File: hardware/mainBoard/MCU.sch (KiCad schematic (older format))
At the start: 7 parts

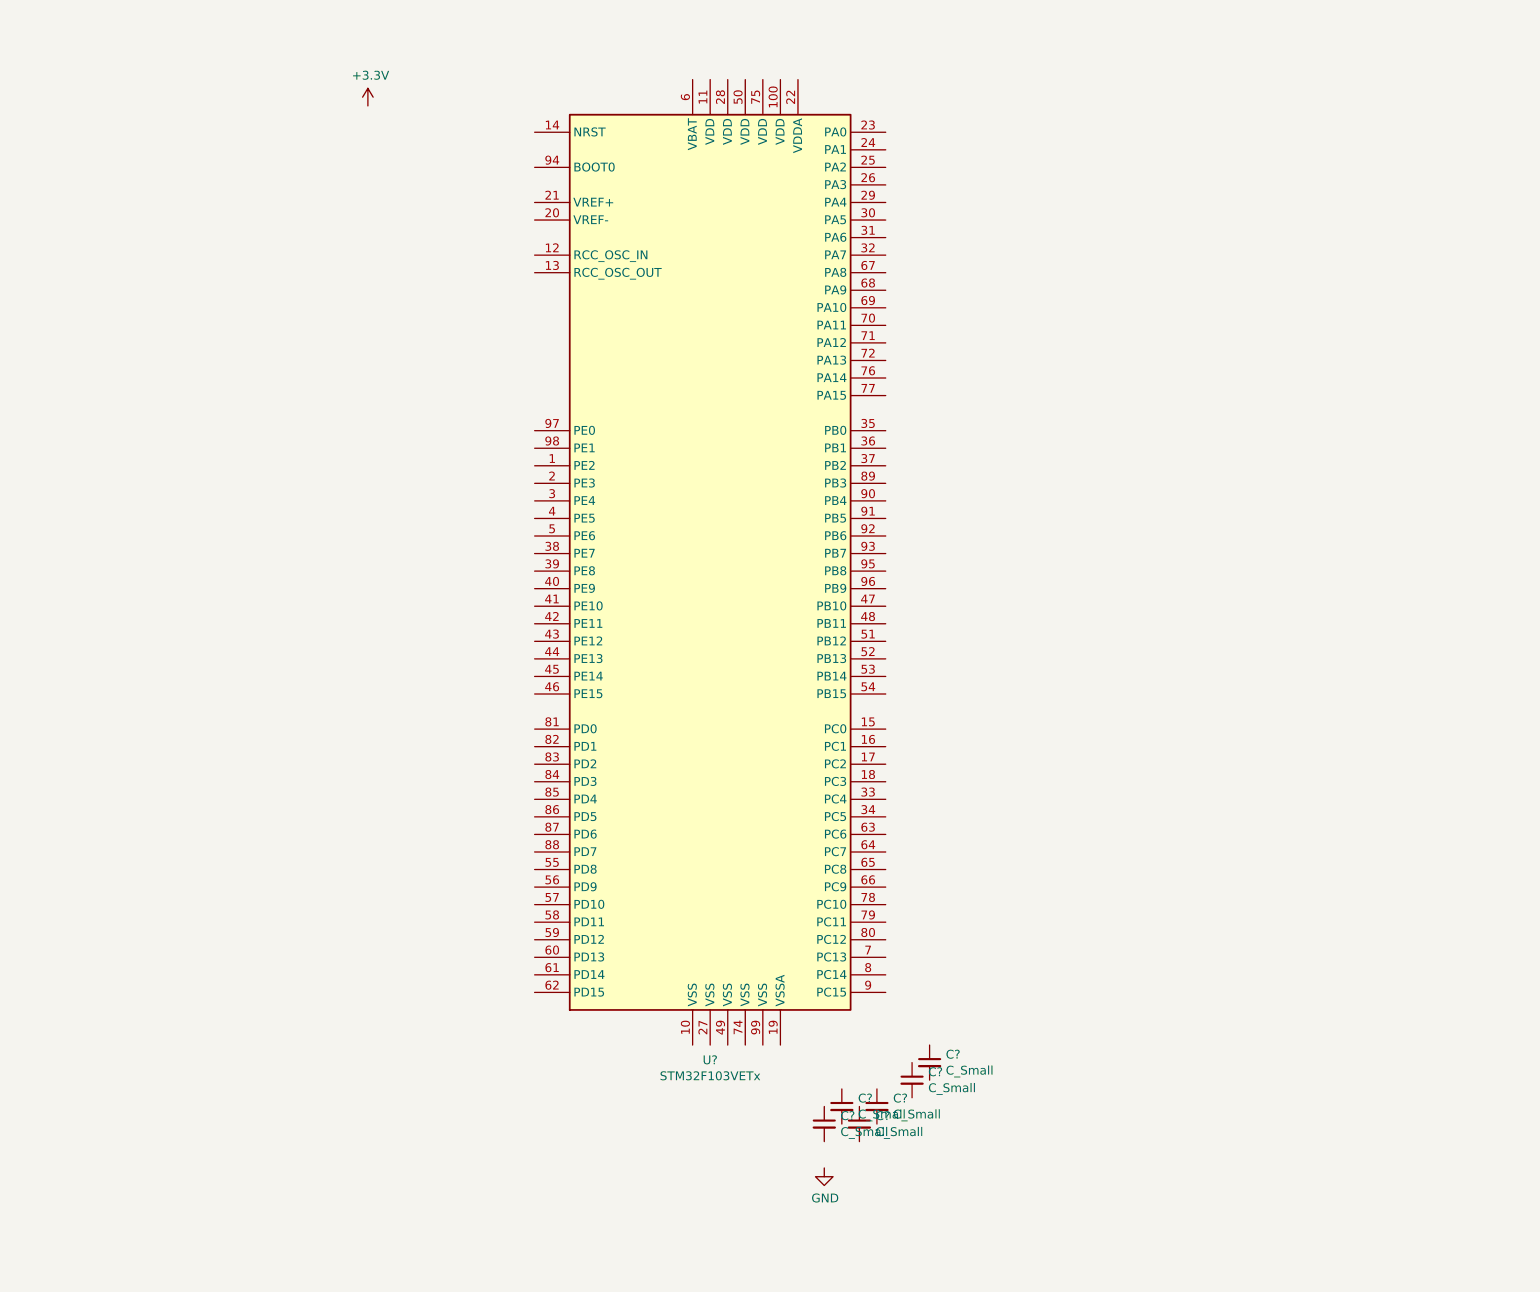
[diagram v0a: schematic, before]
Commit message: Added the power part of the schematic
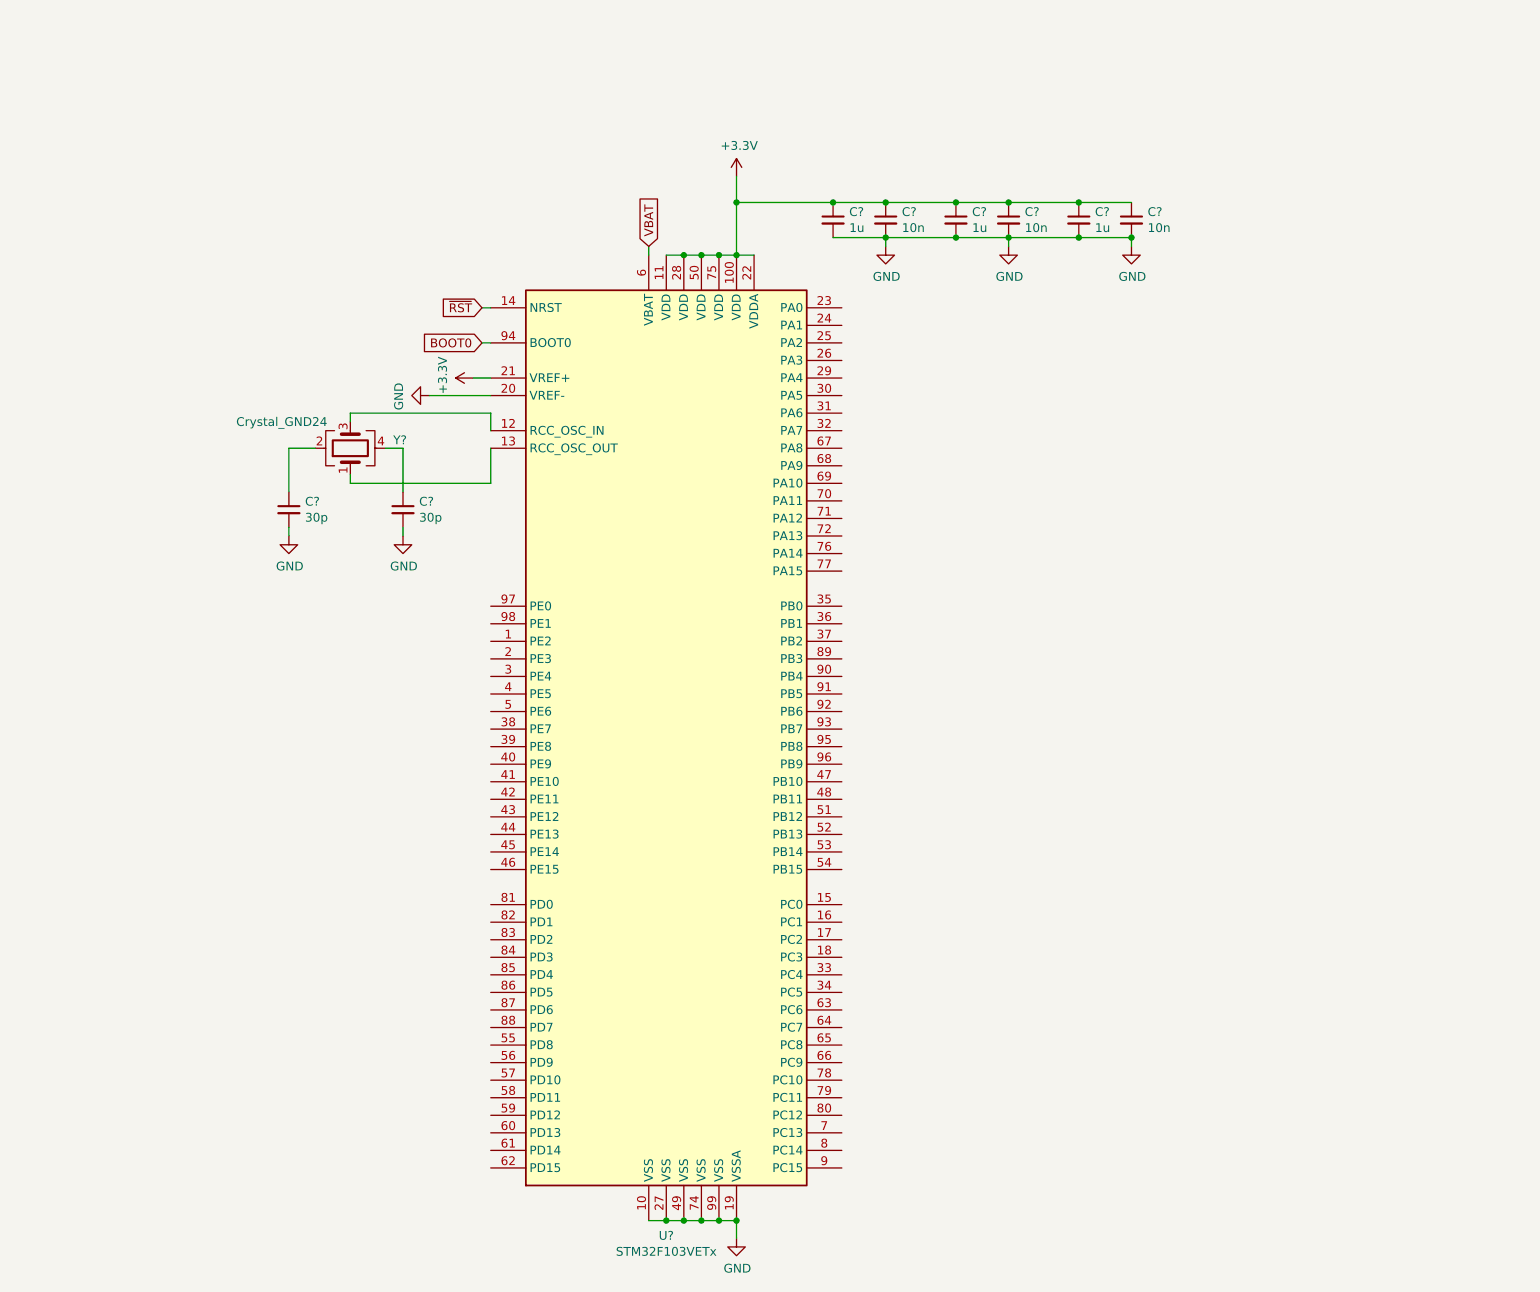
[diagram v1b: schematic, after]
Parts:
- removed C? (x5): C_Small, symbol Device:C_Small
- added C? (x3): 10n, symbol Device:C_Small
- added C? (x2): 1u, symbol Device:C_Small
- added C? (x2): 30p, symbol Device:C_Small
- added Y?: Crystal_GND24, symbol Device:Crystal_GND24
- C?: value C_Small -> 1u
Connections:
- net +3V3: now also C?.1, U?.100 (VDD), U?.11 (VDD), U?.21 (VREF+), U?.22 (VDDA), U?.28 (VDD), U?.50 (VDD), U?.75 (VDD), C?.1, C?.1, C?.1, C?.1, C?.1
- net GND: now also C?.2, U?.10 (VSS), U?.19 (VSSA), U?.20 (VREF-), U?.27 (VSS), U?.49 (VSS), U?.74 (VSS), U?.99 (VSS), C?.2, C?.2, C?.2, C?.2, C?.2, C?.2, C?.2
- net at U?.12 (RCC_OSC_IN): now also Y?.3
- net at U?.13 (RCC_OSC_OUT): now also Y?.1
- net ~RST: now reaches U?.14 (NRST)
- net VBAT: now reaches U?.6 (VBAT)
- net BOOT0: now reaches U?.94 (BOOT0)
- new net: C?.1, Y?.2
- new net: C?.1, Y?.4
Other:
- moved on the sheet: C?, U?

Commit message: Added external connections, analog conditioning and several items
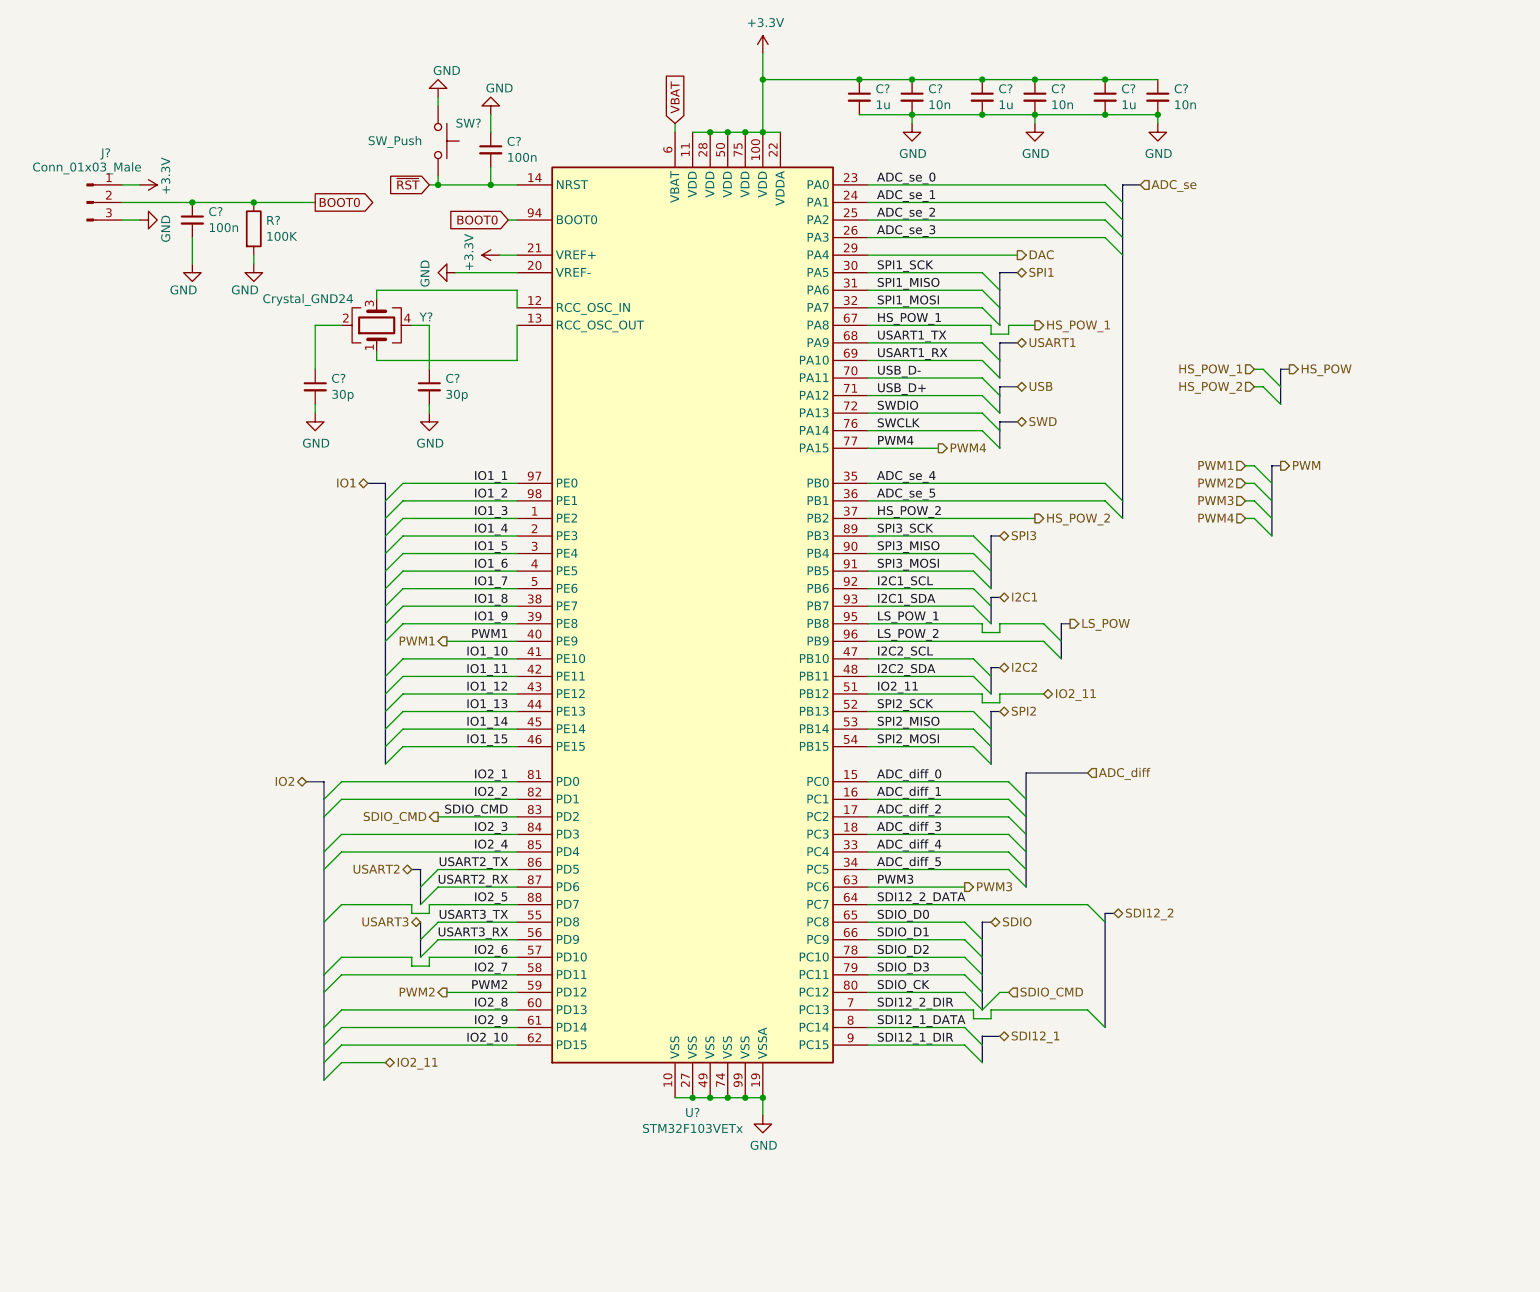
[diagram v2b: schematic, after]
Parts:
- added C? (x2): 100n, symbol Device:C_Small
- added J?: Conn_01x03_Male, symbol Connector:Conn_01x03_Male
- added R?: 100K, symbol Device:R
- added SW?: SW_Push, symbol Switch:SW_Push
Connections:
- net +3V3: now also J?.1 (Pin_1)
- net BOOT0: now also C?.1, J?.2 (Pin_2), R?.1
- net GND: now also C?.1, C?.2, J?.3 (Pin_3), R?.2, SW?.1
- net ~RST: now also C?.2, SW?.2
- net IO1_3: now reaches U?.1 (PE2)
- net ADC_diff_0: now reaches U?.15 (PC0)
- net ADC_diff_1: now reaches U?.16 (PC1)
- net ADC_diff_2: now reaches U?.17 (PC2)
- net ADC_diff_3: now reaches U?.18 (PC3)
- net IO1_4: now reaches U?.2 (PE3)
- net ADC_se_0: now reaches U?.23 (PA0)
- net ADC_se_1: now reaches U?.24 (PA1)
- net ADC_se_2: now reaches U?.25 (PA2)
- net ADC_se_3: now reaches U?.26 (PA3)
- net DAC: now reaches U?.29 (PA4)
- net IO1_5: now reaches U?.3 (PE4)
- net SPI1_SCK: now reaches U?.30 (PA5)
- net SPI1_MISO: now reaches U?.31 (PA6)
- net SPI1_MOSI: now reaches U?.32 (PA7)
- net ADC_diff_4: now reaches U?.33 (PC4)
- net ADC_diff_5: now reaches U?.34 (PC5)
- net ADC_se_4: now reaches U?.35 (PB0)
- net ADC_se_5: now reaches U?.36 (PB1)
- net HS_POW_2: now reaches U?.37 (PB2)
- net IO1_8: now reaches U?.38 (PE7)
- net IO1_9: now reaches U?.39 (PE8)
- net IO1_6: now reaches U?.4 (PE5)
- net PWM1: now reaches U?.40 (PE9)
- net IO1_10: now reaches U?.41 (PE10)
- net IO1_11: now reaches U?.42 (PE11)
- net IO1_12: now reaches U?.43 (PE12)
- net IO1_13: now reaches U?.44 (PE13)
- net IO1_14: now reaches U?.45 (PE14)
- net IO1_15: now reaches U?.46 (PE15)
- net I2C2_SCL: now reaches U?.47 (PB10)
- net I2C2_SDA: now reaches U?.48 (PB11)
- net IO1_7: now reaches U?.5 (PE6)
- net IO2_11: now reaches U?.51 (PB12)
- net SPI2_SCK: now reaches U?.52 (PB13)
- net SPI2_MISO: now reaches U?.53 (PB14)
- net SPI2_MOSI: now reaches U?.54 (PB15)
- net USART3_TX: now reaches U?.55 (PD8)
- net USART3_RX: now reaches U?.56 (PD9)
- net IO2_6: now reaches U?.57 (PD10)
- net IO2_7: now reaches U?.58 (PD11)
- net PWM2: now reaches U?.59 (PD12)
- net IO2_8: now reaches U?.60 (PD13)
- net IO2_9: now reaches U?.61 (PD14)
- net IO2_10: now reaches U?.62 (PD15)
- net PWM3: now reaches U?.63 (PC6)
- net SDI12_2_DATA: now reaches U?.64 (PC7)
- net SDIO_D0: now reaches U?.65 (PC8)
- net SDIO_D1: now reaches U?.66 (PC9)
- net HS_POW_1: now reaches U?.67 (PA8)
- net USART1_TX: now reaches U?.68 (PA9)
- net USART1_RX: now reaches U?.69 (PA10)
- net SDI12_2_DIR: now reaches U?.7 (PC13)
- net USB_D-: now reaches U?.70 (PA11)
- net USB_D+: now reaches U?.71 (PA12)
- net SWDIO: now reaches U?.72 (PA13)
- net SWCLK: now reaches U?.76 (PA14)
- net PWM4: now reaches U?.77 (PA15)
- net SDIO_D2: now reaches U?.78 (PC10)
- net SDIO_D3: now reaches U?.79 (PC11)
- net SDI12_1_DATA: now reaches U?.8 (PC14)
- net SDIO_CK: now reaches U?.80 (PC12)
- net IO2_1: now reaches U?.81 (PD0)
- net IO2_2: now reaches U?.82 (PD1)
- net SDIO_CMD: now reaches U?.83 (PD2)
- net IO2_3: now reaches U?.84 (PD3)
- net IO2_4: now reaches U?.85 (PD4)
- net USART2_TX: now reaches U?.86 (PD5)
- net USART2_RX: now reaches U?.87 (PD6)
- net IO2_5: now reaches U?.88 (PD7)
- net SPI3_SCK: now reaches U?.89 (PB3)
- net SDI12_1_DIR: now reaches U?.9 (PC15)
- net SPI3_MISO: now reaches U?.90 (PB4)
- net SPI3_MOSI: now reaches U?.91 (PB5)
- net I2C1_SCL: now reaches U?.92 (PB6)
- net I2C1_SDA: now reaches U?.93 (PB7)
- net LS_POW_1: now reaches U?.95 (PB8)
- net LS_POW_2: now reaches U?.96 (PB9)
- net IO1_1: now reaches U?.97 (PE0)
- net IO1_2: now reaches U?.98 (PE1)
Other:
- moved on the sheet: C?, U?, Y?
